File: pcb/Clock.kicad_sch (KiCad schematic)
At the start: 19 parts, among them Y3 Si5351C-B-GM, Y4 3225-25M-SR

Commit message: Clock rounting
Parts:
- removed R23, R24, R25, R26, R27, R28, R29, R30: 0R, Resistor_SMD:R_0402_1005Metric_Pad0.72x0.64mm_HandSolder, symbol Device:R
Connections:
- net CLK0: now also Y3.13 (CLK0)
- net CLK1: now also Y3.12 (CLK1)
- net CLK2: now also Y3.9 (CLK2)
- net CLK3: now also Y3.8 (CLK3)
- net CLK4: now also Y3.19 (CLK4)
- net CLK5: now also Y3.17 (CLK5)
- net CLK6: now also Y3.16 (CLK6)
- net CLK7: now also Y3.15 (CLK7)

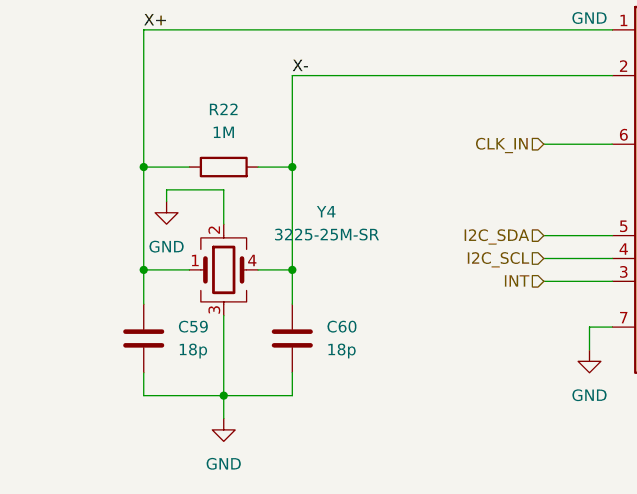
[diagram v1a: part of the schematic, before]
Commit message: Crystal footprint changed, routing and eth trafo to correct
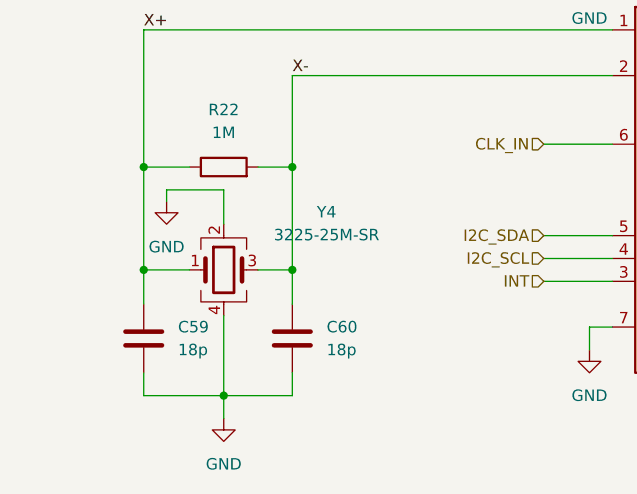
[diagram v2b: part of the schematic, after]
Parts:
- Y4: symbol Device:Crystal_GND23 -> Device:Crystal_GND24
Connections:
- net GND: now also Y4.4; no longer Y4.3
- net X-: now also Y4.3; no longer Y4.4
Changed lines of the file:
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@@
 	)
 	(symbol
-		(lib_id "Device:Crystal_GND23")
+		(lib_id "Device:Crystal_GND24")
 		(at 68.58 95.25 0)
 		(unit 1)
@@
 			)
 		)
-		(property "Description" "Four pin crystal, GND on pins 2 and 3"
+		(property "Description" "Four pin crystal, GND on pins 2 and 4"
 			(at 68.58 95.25 0)
 			(effects
